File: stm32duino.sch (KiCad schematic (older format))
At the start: 19 parts, among them P1 RF7021SE, P2 DISP_I2C, P3 DISP_SER, P4 HOST_SER, U1 stm32f103c8t6-module-china

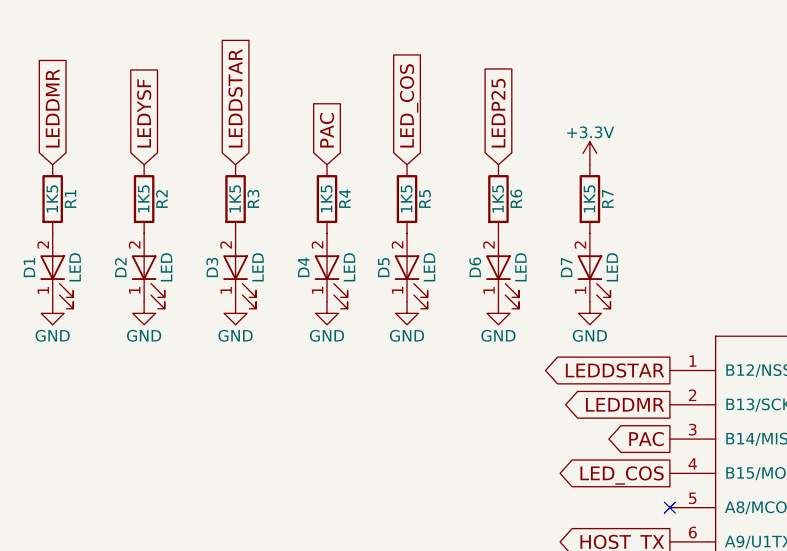
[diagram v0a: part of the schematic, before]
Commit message: Moved LEDs around, grouped them by logical function.
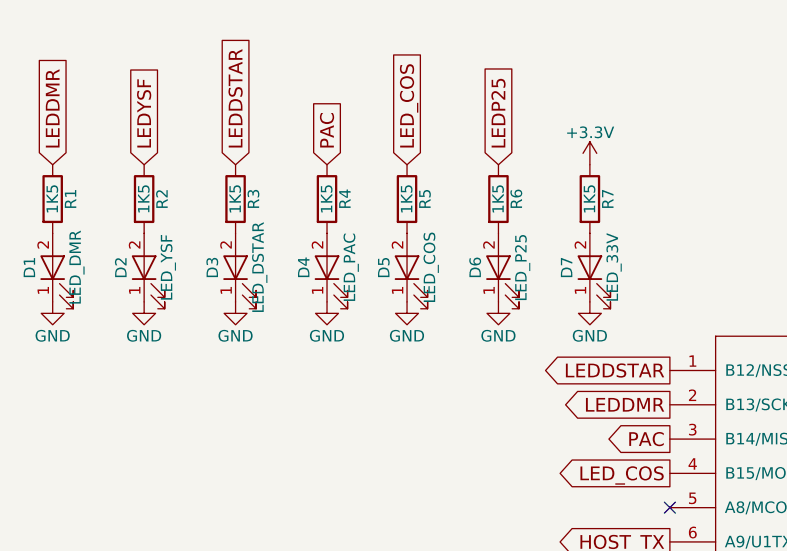
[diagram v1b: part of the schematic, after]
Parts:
- D1: value LED -> LED_DMR
- D2: value LED -> LED_YSF
- D3: value LED -> LED_DSTAR
- D4: value LED -> LED_PAC
- D5: value LED -> LED_COS
- D6: value LED -> LED_P25
- D7: value LED -> LED_33V
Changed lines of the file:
@@
 P 1400 1450
 F 0 "D1" H 1400 1550 50  0000 C CNN
-F 1 "LED" H 1400 1350 50  0000 C CNN
+F 1 "LED_DMR" H 1400 1350 50  0000 C CNN
 F 2 "LEDs:LED_0805" H 1400 1450 50  0001 C CNN
 F 3 "" H 1400 1450 50  0000 C CNN
@@
 P 1800 1450
 F 0 "D2" H 1800 1550 50  0000 C CNN
-F 1 "LED" H 1800 1350 50  0000 C CNN
+F 1 "LED_YSF" H 1800 1350 50  0000 C CNN
 F 2 "LEDs:LED_0805" H 1800 1450 50  0001 C CNN
 F 3 "" H 1800 1450 50  0000 C CNN
@@
 P 2200 1450
 F 0 "D3" H 2200 1550 50  0000 C CNN
-F 1 "LED" H 2200 1350 50  0000 C CNN
+F 1 "LED_DSTAR" H 2200 1350 50  0000 C CNN
 F 2 "LEDs:LED_0805" H 2200 1450 50  0001 C CNN
 F 3 "" H 2200 1450 50  0000 C CNN
@@
 P 2600 1450
 F 0 "D4" H 2600 1550 50  0000 C CNN
-F 1 "LED" H 2600 1350 50  0000 C CNN
+F 1 "LED_PAC" H 2600 1350 50  0000 C CNN
 F 2 "LEDs:LED_0805" H 2600 1450 50  0001 C CNN
 F 3 "" H 2600 1450 50  0000 C CNN
@@
 P 2950 1450
 F 0 "D5" H 2950 1550 50  0000 C CNN
-F 1 "LED" H 2950 1350 50  0000 C CNN
+F 1 "LED_COS" H 2950 1350 50  0000 C CNN
 F 2 "LEDs:LED_0805" H 2950 1450 50  0001 C CNN
 F 3 "" H 2950 1450 50  0000 C CNN
@@
 P 3350 1450
 F 0 "D6" H 3350 1550 50  0000 C CNN
-F 1 "LED" H 3350 1350 50  0000 C CNN
+F 1 "LED_P25" H 3350 1350 50  0000 C CNN
 F 2 "LEDs:LED_0805" H 3350 1450 50  0001 C CNN
 F 3 "" H 3350 1450 50  0000 C CNN
@@
 P 3750 1450
 F 0 "D7" H 3750 1550 50  0000 C CNN
-F 1 "LED" H 3750 1350 50  0000 C CNN
+F 1 "LED_33V" H 3750 1350 50  0000 C CNN
 F 2 "LEDs:LED_0805" H 3750 1450 50  0001 C CNN
 F 3 "" H 3750 1450 50  0000 C CNN
